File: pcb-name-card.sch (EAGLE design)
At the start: 8 parts, among them U1 3V, U2 3V

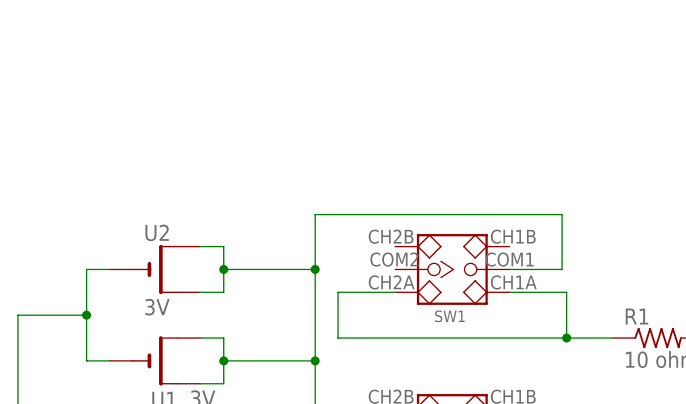
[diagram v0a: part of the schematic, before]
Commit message: support nfc band
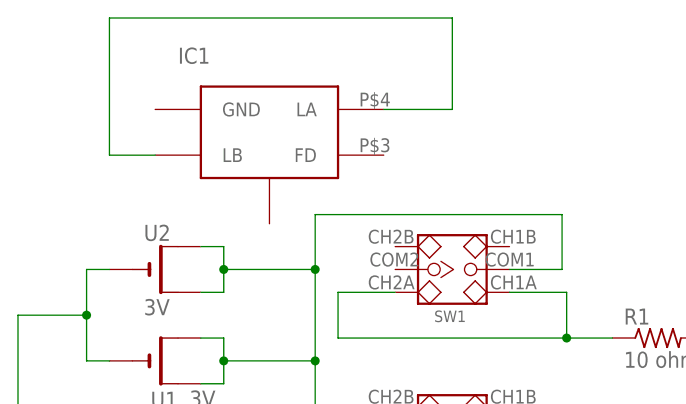
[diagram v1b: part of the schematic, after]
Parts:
- added IC1: NTAG21XFDRC-FIT, ntag21xf:NTAG21XFDRC-FIT
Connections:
- new net N$6: IC1.LA, IC1.LB
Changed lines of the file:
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@@
 <?xml version="1.0" encoding="utf-8"?>
 <!DOCTYPE eagle SYSTEM "eagle.dtd">
-<eagle version="7.3.0">
+<eagle version="7.5.0">
 <drawing>
 <settings>
@@
 <part name="R1" library="resistor" deviceset="R-US_" device="R2010" value="10 ohm"/>
 <part name="R2" library="resistor" deviceset="R-US_" device="R2010" value="330 ohm"/>
+<part name="IC1" library="ntag21xf" deviceset="NTAG21XF" device="DRC-FIT"/>
 </parts>
 <sheets>
@@
 <instance part="R1" gate="G$1" x="81.28" y="93.98"/>
 <instance part="R2" gate="G$1" x="81.28" y="81.28"/>
+<instance part="IC1" gate="G$1" x="38.1" y="116.84"/>
 </instances>
 <busses>
@@
 </segment>
 </net>
+<net name="N$6" class="0">
+<segment>
+<pinref part="IC1" gate="G$1" pin="LA"/>
+<wire x1="50.8" y1="119.38" x2="58.42" y2="119.38" width="0.1524" layer="91"/>
+<wire x1="58.42" y1="119.38" x2="58.42" y2="129.54" width="0.1524" layer="91"/>
+<wire x1="58.42" y1="129.54" x2="20.32" y2="129.54" width="0.1524" layer="91"/>
+<wire x1="20.32" y1="129.54" x2="20.32" y2="114.3" width="0.1524" layer="91"/>
+<pinref part="IC1" gate="G$1" pin="LB"/>
+<wire x1="20.32" y1="114.3" x2="25.4" y2="114.3" width="0.1524" layer="91"/>
+</segment>
+</net>

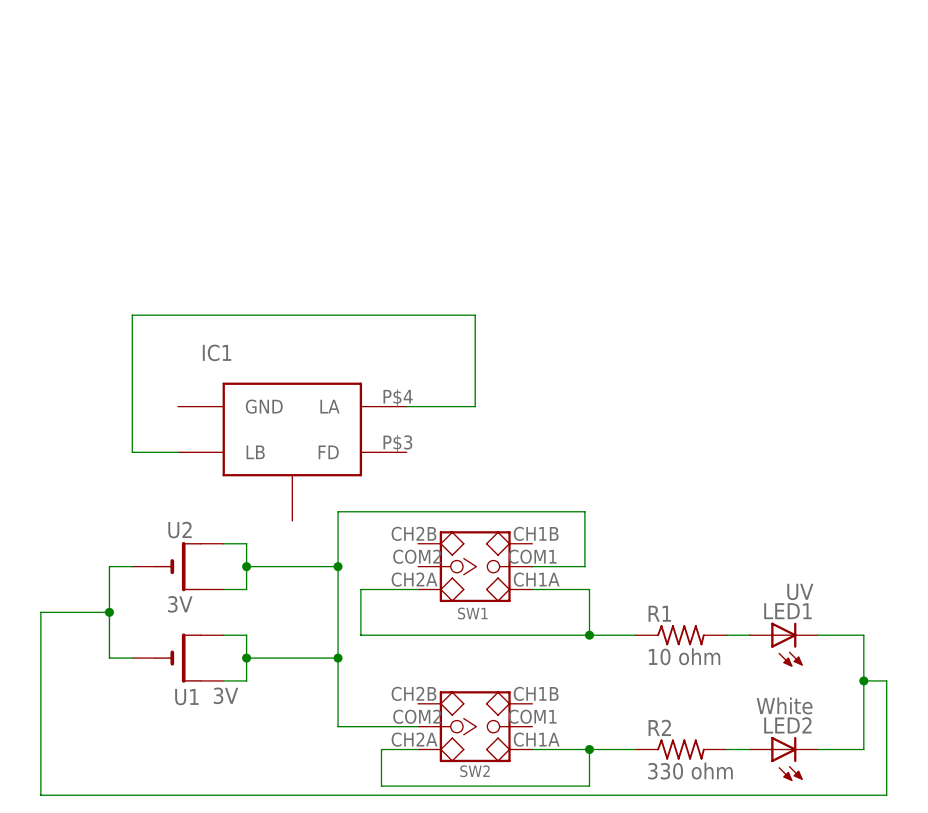
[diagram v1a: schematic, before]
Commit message: use ntag i2c
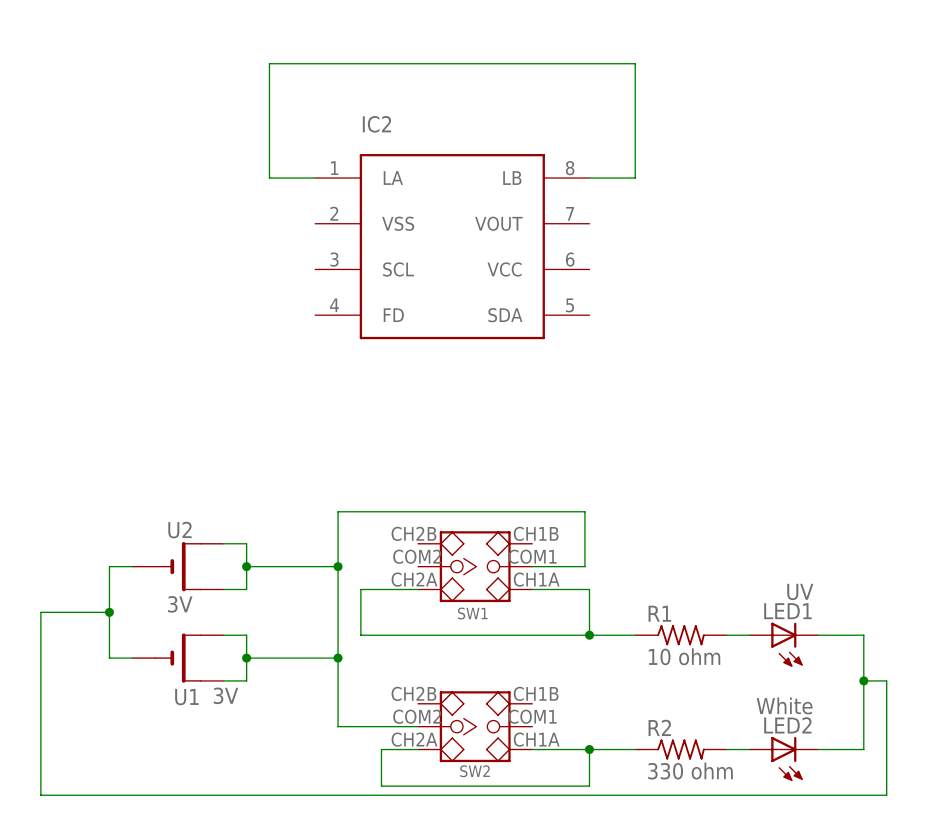
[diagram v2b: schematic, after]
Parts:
- removed IC1: NTAG21XFDRC-FIT, ntag21xf:NTAG21XFDRC-FIT
- added IC2: NT3H1X01W0FTT, ntagi2c:NT3H1X01W0FTT
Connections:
- net N$6: now also IC2.LA, IC2.LB; no longer IC1.LA, IC1.LB
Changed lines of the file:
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@@
 <part name="R1" library="resistor" deviceset="R-US_" device="R2010" value="10 ohm"/>
 <part name="R2" library="resistor" deviceset="R-US_" device="R2010" value="330 ohm"/>
-<part name="IC1" library="ntag21xf" deviceset="NTAG21XF" device="DRC-FIT"/>
+<part name="IC2" library="ntagi2c" deviceset="NT3H1X01" device="W0FTT"/>
 </parts>
 <sheets>
@@
 <instance part="R1" gate="G$1" x="81.28" y="93.98"/>
 <instance part="R2" gate="G$1" x="81.28" y="81.28"/>
-<instance part="IC1" gate="G$1" x="38.1" y="116.84"/>
+<instance part="IC2" gate="G$1" x="55.88" y="137.16"/>
 </instances>
 <busses>
@@
 <net name="N$6" class="0">
 <segment>
-<pinref part="IC1" gate="G$1" pin="LA"/>
-<wire x1="50.8" y1="119.38" x2="58.42" y2="119.38" width="0.1524" layer="91"/>
-<wire x1="58.42" y1="119.38" x2="58.42" y2="129.54" width="0.1524" layer="91"/>
-<wire x1="58.42" y1="129.54" x2="20.32" y2="129.54" width="0.1524" layer="91"/>
-<wire x1="20.32" y1="129.54" x2="20.32" y2="114.3" width="0.1524" layer="91"/>
-<pinref part="IC1" gate="G$1" pin="LB"/>
-<wire x1="20.32" y1="114.3" x2="25.4" y2="114.3" width="0.1524" layer="91"/>
+<pinref part="IC2" gate="G$1" pin="LA"/>
+<wire x1="40.64" y1="144.78" x2="35.56" y2="144.78" width="0.1524" layer="91"/>
+<wire x1="35.56" y1="144.78" x2="35.56" y2="157.48" width="0.1524" layer="91"/>
+<wire x1="35.56" y1="157.48" x2="76.2" y2="157.48" width="0.1524" layer="91"/>
+<wire x1="76.2" y1="157.48" x2="76.2" y2="144.78" width="0.1524" layer="91"/>
+<pinref part="IC2" gate="G$1" pin="LB"/>
+<wire x1="76.2" y1="144.78" x2="71.12" y2="144.78" width="0.1524" layer="91"/>
 </segment>
 </net>

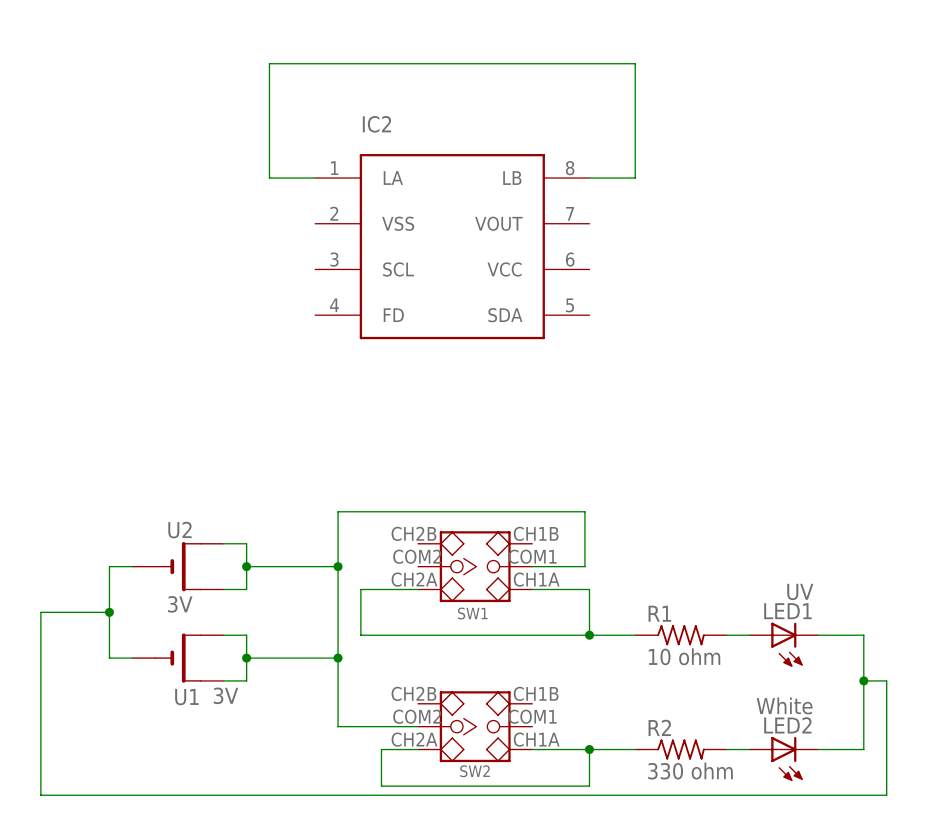
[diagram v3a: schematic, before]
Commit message: combine both tag footprints on design
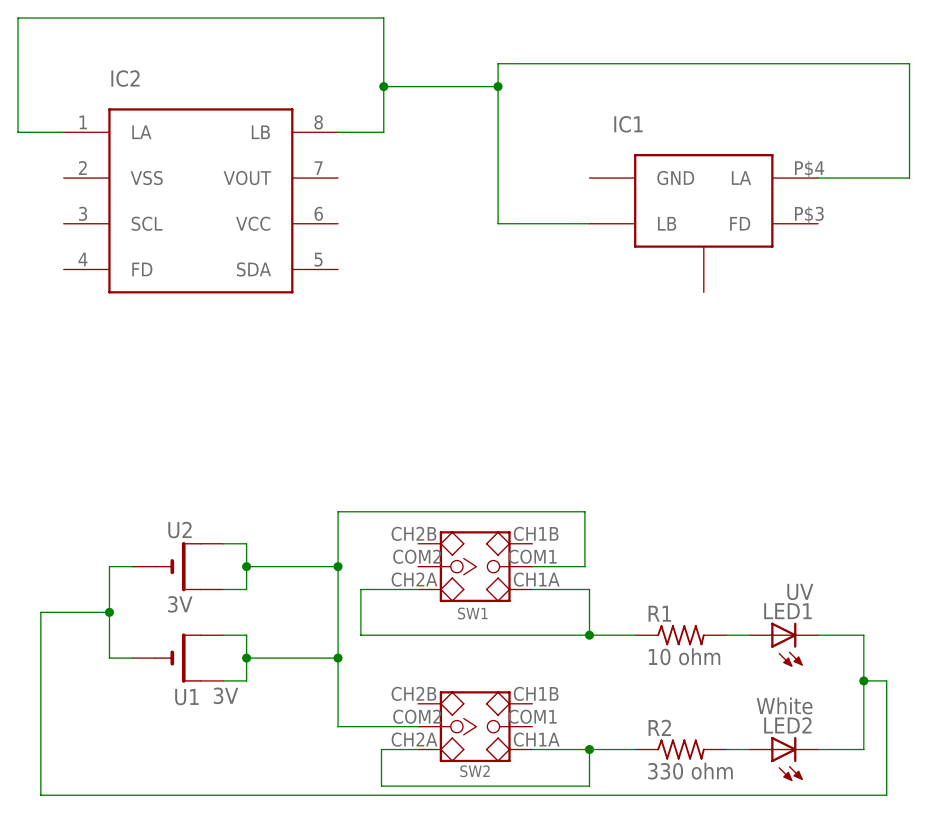
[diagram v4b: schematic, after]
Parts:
- added IC1: NTAG21XFDRC-FIT, ntag21xf:NTAG21XFDRC-FIT
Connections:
- net N$6: now also IC1.LA, IC1.LB
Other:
- moved on the sheet: IC2
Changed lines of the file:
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@@
 <part name="R2" library="resistor" deviceset="R-US_" device="R2010" value="330 ohm"/>
 <part name="IC2" library="ntagi2c" deviceset="NT3H1X01" device="W0FTT"/>
+<part name="IC1" library="ntag21xf" deviceset="NTAG21XF" device="DRC-FIT"/>
 </parts>
 <sheets>
@@
 <instance part="R1" gate="G$1" x="81.28" y="93.98"/>
 <instance part="R2" gate="G$1" x="81.28" y="81.28"/>
-<instance part="IC2" gate="G$1" x="55.88" y="137.16"/>
+<instance part="IC2" gate="G$1" x="27.94" y="142.24"/>
+<instance part="IC1" gate="G$1" x="83.82" y="142.24"/>
 </instances>
 <busses>
@@
 <segment>
 <pinref part="IC2" gate="G$1" pin="LA"/>
-<wire x1="40.64" y1="144.78" x2="35.56" y2="144.78" width="0.1524" layer="91"/>
-<wire x1="35.56" y1="144.78" x2="35.56" y2="157.48" width="0.1524" layer="91"/>
-<wire x1="35.56" y1="157.48" x2="76.2" y2="157.48" width="0.1524" layer="91"/>
-<wire x1="76.2" y1="157.48" x2="76.2" y2="144.78" width="0.1524" layer="91"/>
+<wire x1="12.7" y1="149.86" x2="7.62" y2="149.86" width="0.1524" layer="91"/>
+<wire x1="7.62" y1="149.86" x2="7.62" y2="162.56" width="0.1524" layer="91"/>
+<wire x1="7.62" y1="162.56" x2="48.26" y2="162.56" width="0.1524" layer="91"/>
+<wire x1="48.26" y1="162.56" x2="48.26" y2="154.94" width="0.1524" layer="91"/>
 <pinref part="IC2" gate="G$1" pin="LB"/>
-<wire x1="76.2" y1="144.78" x2="71.12" y2="144.78" width="0.1524" layer="91"/>
+<wire x1="48.26" y1="154.94" x2="48.26" y2="149.86" width="0.1524" layer="91"/>
+<wire x1="48.26" y1="149.86" x2="43.18" y2="149.86" width="0.1524" layer="91"/>
+<pinref part="IC1" gate="G$1" pin="LA"/>
+<wire x1="96.52" y1="144.78" x2="106.68" y2="144.78" width="0.1524" layer="91"/>
+<wire x1="106.68" y1="144.78" x2="106.68" y2="157.48" width="0.1524" layer="91"/>
+<wire x1="106.68" y1="157.48" x2="60.96" y2="157.48" width="0.1524" layer="91"/>
+<wire x1="60.96" y1="157.48" x2="60.96" y2="154.94" width="0.1524" layer="91"/>
+<pinref part="IC1" gate="G$1" pin="LB"/>
+<wire x1="60.96" y1="154.94" x2="60.96" y2="139.7" width="0.1524" layer="91"/>
+<wire x1="60.96" y1="139.7" x2="71.12" y2="139.7" width="0.1524" layer="91"/>
+<wire x1="48.26" y1="154.94" x2="60.96" y2="154.94" width="0.1524" layer="91"/>
+<junction x="48.26" y="154.94"/>
+<junction x="60.96" y="154.94"/>
 </segment>
 </net>
